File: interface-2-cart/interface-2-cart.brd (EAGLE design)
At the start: 49.5 x 47.9 mm, 37 parts, among them U1 RP2040, U2 SN74LVC245ADBR, U3 W25Q128JVSIQ, U4 SN74LVC245ADBR, U5 SN74LVC245ADBR, X1 TSX-32250

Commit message: New images
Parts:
- added PROG: (no value), adafruit:1X06
- added Q1, Q2: (no value), semicon-smd-ipc:SOT23
- added R1, R10, R11, R12, R13, R14, R15, R16, R17, R18, R19, R2, R20, R5: 1K, rcl:R0402
- added R4, R6: 10K, rcl:R0402
- added RST_BUT: PTS645SM43SMTR92LFS, PTS645SM43SMTR92LFS:PTS645(SMT)
- added S_LED1, S_LED10, S_LED2, S_LED3, S_LED362, S_LED4, S_LED5, S_LED6, S_LED7, S_LED8, S_LED9: 20mA, led-0402:LED_VLMW15_VIS
- moved C2 11.8 mm to (13.5, 15.5)
- moved C3 11.8 mm to (13.6, 27.3)
- moved 3V3_REG2 11.8 mm to (33.8, 29.1)
- moved C11 11.8 mm to (33.8, 26.2)
- moved C8 11.8 mm to (33.8, 32.0)
- moved R9 4.59 mm to (36.3, 34.8), turned to 90 degrees
- moved C18 3.42 mm to (1.52, 29.0), turned to 90 degrees
- moved R8 2.97 mm to (36.2, 43.2), turned to 90 degrees
- moved RUN_BUT 1.91 mm to (41.8, 34.5)
- moved C5 0.64 mm to (24.4, 36.4)
- moved X1 0.64 mm to (23.7, 32.5)
- moved C1 0.63 mm to (26.9, 32.9)
- moved C9 0.63 mm to (22.1, 36.2)
- moved BOOT_BUT 0.51 mm to (41.7, 43.2)
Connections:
- removed net BUT: U1.34
- removed net RESET_5V: U5.2
- removed net ROMCS: U1.39, U2.1
- new net /CARTCS: R1.1, R6.2, S_LED8.C, U1.39
- new net /RESET: PROG.4, Q2.3, R4.2, RST_BUT.3
- new net CARTCS: Q1.3, R5.2, U$1./ROMCS, U2.1
- new net L0: R10.1, S_LED7.A
- new net L1: R11.1, S_LED6.A
- new net L2: R12.1, S_LED5.A
- new net L3: R13.1, S_LED4.A
- new net L4: R14.1, S_LED3.A
- new net L5: R15.1, S_LED2.A
- new net L6: R16.1, S_LED1.A
- new net L7: R17.1, S_LED362.A
- new net N$1: Q1.1, R1.2
- new net N$2: Q2.1, R2.2
- new net N$4: R18.1, S_LED8.A
- new net N$5: R19.1, S_LED9.A
- new net N$6: R20.1, S_LED10.A
- new net SWCLK: PROG.2, U1.24
- new net SWD: PROG.3, U1.25
- new net USER_LED: R20.2, U1.34
- net 3V3: now also PROG.1, R6.1; no longer C2.2, U2.20
- net D0: now also R10.2
- net D1: now also R11.2
- net D2: now also R12.2
- net D3: now also R13.2
- net D4: now also R14.2
- net D5: now also R15.2
- net D6: now also R16.2
- net D7: now also R17.2
- net GND: now also PROG.6, Q1.2, Q2.2, RST_BUT.1, S_LED1.C, S_LED10.C, S_LED2.C, S_LED3.C, S_LED362.C, S_LED4.C, S_LED5.C, S_LED6.C, S_LED7.C, U5.18
- net RESET: now also R2.1; no longer U5.18
- net ROMRQ_5V: now also S_LED9.C
- net VCC: now also C2.2, PROG.5, R18.2, R19.2, R4.1, R5.1, U2.20; no longer U$1./ROMCS
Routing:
- net CARTCS: track 0.00 -> 65.1 mm, vias 0 -> 2
- net USER_LED: track 0.00 -> 61.4 mm, vias 0 -> 4
- net /CARTCS: track 0.00 -> 51.3 mm, vias 0 -> 2
- net VCC: track 102.4 -> 61.6 mm, vias 4 -> 8
- net RESET: track 44.4 -> 12.7 mm
- net /RESET: track 0.00 -> 27.0 mm
- net ROMRQ_5V: track 7.15 -> 27.2 mm, vias 0 -> 2
- net GND: track 66.2 -> 86.2 mm, vias 36 -> 40
- net ROMCS: track 18.4 -> 0.00 mm, vias 2 -> 0
- net SWD: track 0.00 -> 13.4 mm
- net D7: track 22.8 -> 36.1 mm
- net L4: track 0.00 -> 12.9 mm, vias 0 -> 2
- net SWCLK: track 0.00 -> 12.6 mm
- net D6: track 24.2 -> 35.7 mm
- net L5: track 0.00 -> 11.5 mm, vias 0 -> 2
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- added copper zone on layer 15, net VCC
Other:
- outline, holes or cut-outs redrawn
- board text added: "/ROMCS"
- board text added: "/ROMRQ"
- board text added: "3V3"
- board text added: "5V"
- board text added: "CLK"
- board text added: "DATA"
- board text added: "GND"
- board text added: "RP BOOT"
- board text added: "RP RUN"
- board text added: "SWD"
- board text added: "USER"
- board text added: "ZX RST"
- board text added: "ZXR"

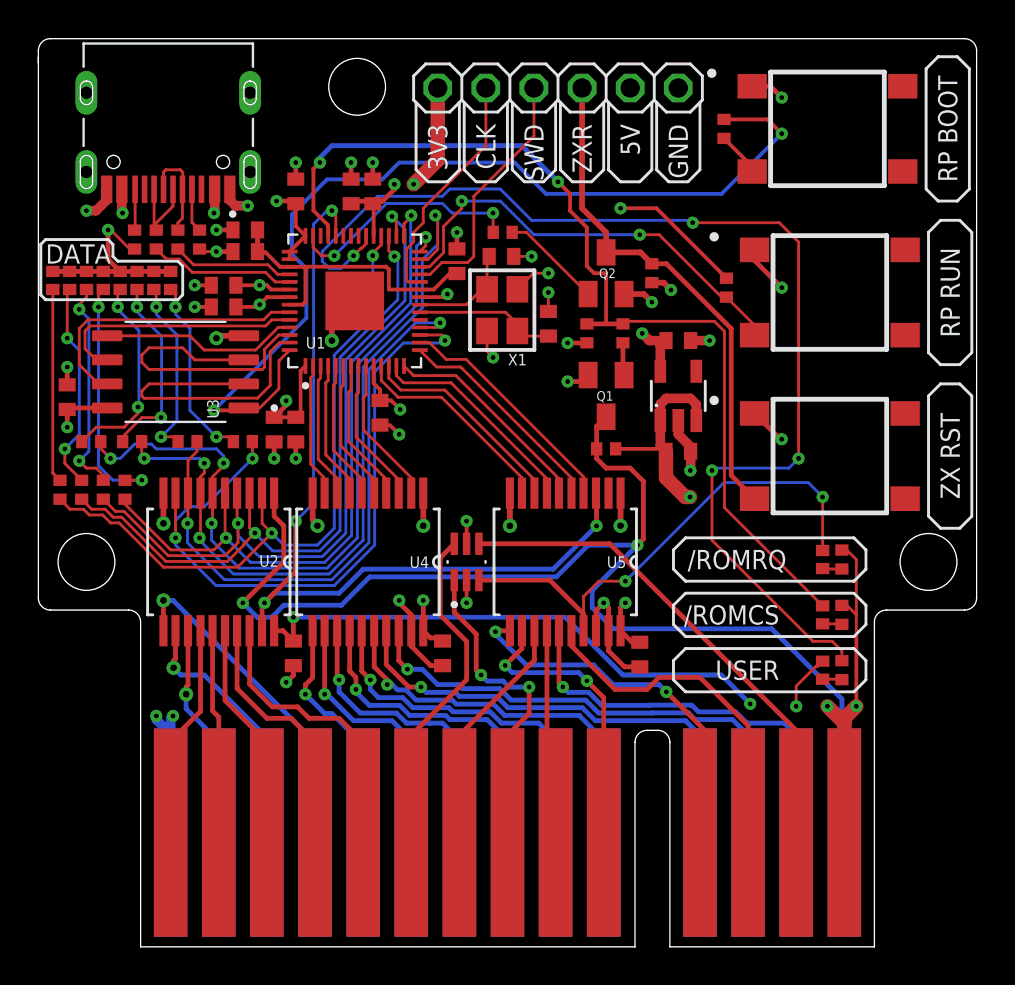
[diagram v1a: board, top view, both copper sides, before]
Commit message: Created initial BOM and mount files, although need to replace one of the octal buffers with a level shifter
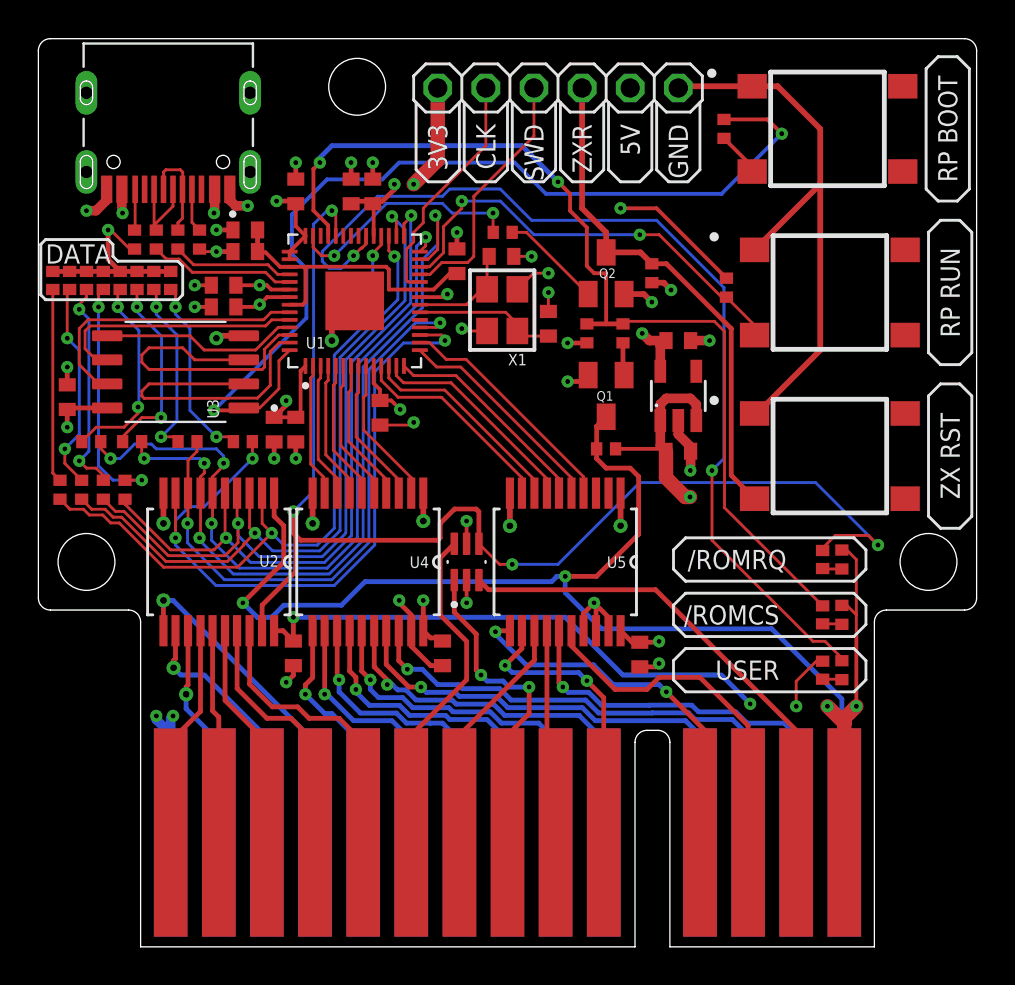
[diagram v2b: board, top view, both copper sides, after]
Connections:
- removed net ROMRQ_5V: S_LED9.C, U$2.3, U5.17
- net A15_5V: now also U$2.3; no longer U$2.4
- net GND: now also U5.17
- net ROMRQ: now also S_LED9.C, U$2.4; no longer U5.3
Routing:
- net ROMRQ_5V: track 27.2 -> 0.00 mm, vias 2 -> 0
- net GND: track 86.2 -> 109.6 mm, vias 40 -> 38
- net ROMRQ: track 46.2 -> 66.2 mm
- net USER_LED: track 61.4 -> 51.8 mm, vias 4 -> 2
- net CARTCS: track 65.1 -> 62.9 mm
- net A15_5V: track 26.2 -> 25.4 mm
- net 3V3: track 52.1 -> 51.6 mm
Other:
- outline, holes or cut-outs redrawn
- board text added: "ZXelerator 2025 Smashcat"

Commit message: Fixed hardware issue! Fixed firmware issue with volatiles not updating - core1 was not starting up!
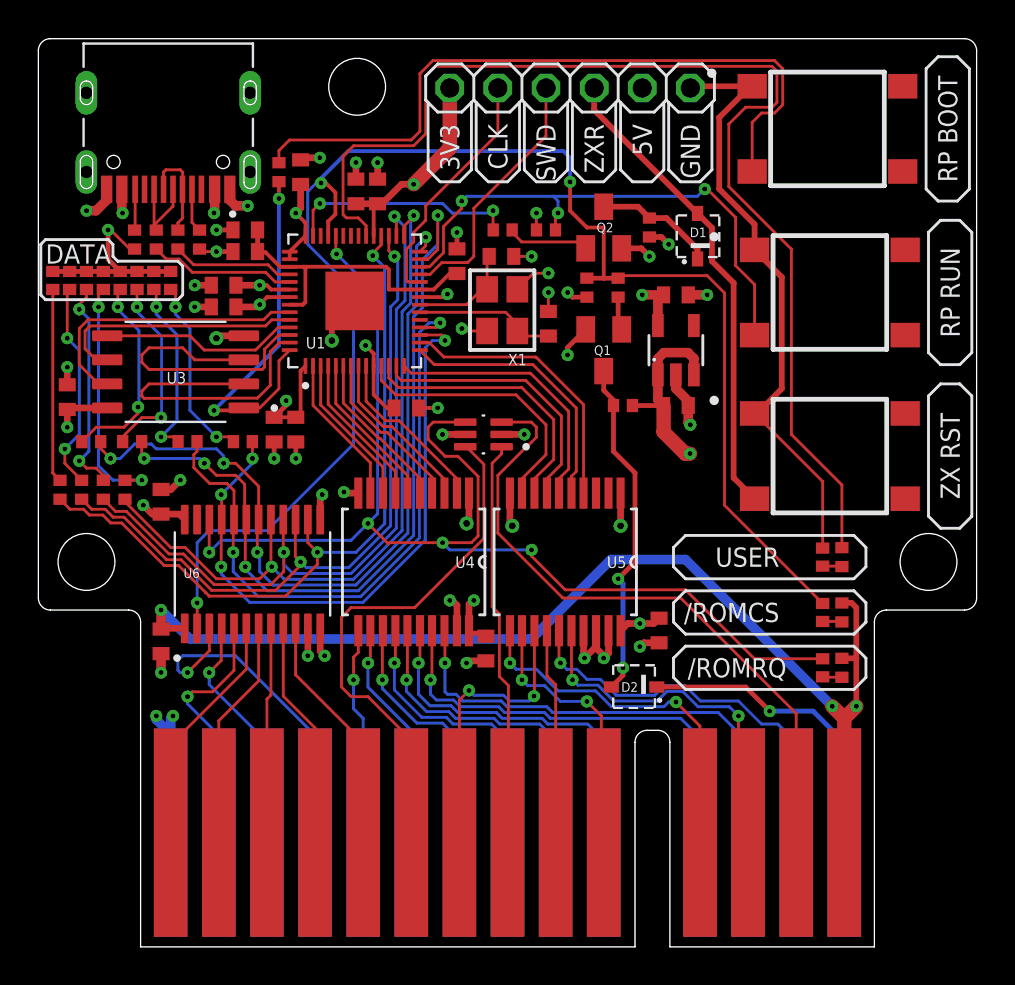
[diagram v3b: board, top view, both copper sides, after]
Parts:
- removed U2: SN74LVC245ADBR, SN74LVC245ADBR:SOP65P780X200-20N
- added C12: 1uF, rcl:C0402
- added D1, D2: BZX384C5V6-E3-08, BZX384C5V6-E3-08:SOD-323
- added U6: SN74LVCC4245APWR, SN74LVCC4245APWR:SOP65P640X120-24N
- R5: value 1K -> 470R
- moved R8 23.6 mm to (12.7, 40.9), turned to 270 degrees
- moved R9 10.0 mm to (26.8, 37.8), turned to 180 degrees
- moved C2 7.01 mm to (6.48, 16.1)
- moved U$2 6.79 mm to (23.5, 27.1), turned to 180 degrees
- moved R20 5.97 mm to (42.4, 20.6)
- moved S_LED10 5.97 mm to (41.4, 20.6)
- moved R19 5.71 mm to (42.4, 14.7)
- moved S_LED9 5.71 mm to (41.4, 14.7)
- moved R5 2.45 mm to (30.9, 28.6)
- moved R1 2.43 mm to (30.6, 34.8)
- moved C8 2.42 mm to (33.7, 34.4)
- moved Q1 2.42 mm to (29.8, 31.5)
- moved 3V3_REG2 2.42 mm to (33.7, 31.5)
- moved C11 2.42 mm to (33.7, 28.6)
- moved Q2 2.42 mm to (29.8, 38.0)
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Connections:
- new net /RESET_PROTECTED: D1.C, Q2.3, R4.2
- new net N$7: D2.C, U$1./ROMCS
- net /CARTCS: now also U6.2
- net /RESET: now also D1.A; no longer Q2.3, R4.2
- net 3V3: now also C12.2, U6.24
- net CARTCS: now also D2.A; no longer U$1./ROMCS, U2.1
- net D0: now also U6.21; no longer U2.9
- net D0_5V: now also U6.3; no longer U2.11
- net D1: now also U6.20; no longer U2.8
- net D1_5V: now also U6.4; no longer U2.12
- net D2: now also U6.19; no longer U2.7
- net D2_5V: now also U6.5; no longer U2.13
- net D3: now also U6.18; no longer U2.6
- net D3_5V: now also U6.6; no longer U2.14
- net D4: now also U6.17; no longer U2.5
- net D4_5V: now also U6.7; no longer U2.15
- net D5: now also U6.16; no longer U2.4
- net D5_5V: now also U6.8; no longer U2.16
- net D6: now also U6.15; no longer U2.3
- net D6_5V: now also U6.9; no longer U2.17
- net D7: now also U6.14; no longer U2.2
- net D7_5V: now also U6.10; no longer U2.18
- net GND: now also C12.1, U6.11, U6.12, U6.13; no longer U2.10
- net ROMRQ: now also U6.22; no longer U2.19
- net VCC: now also U6.1; no longer U2.20
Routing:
- net CARTCS: track 62.9 -> 18.1 mm
- net N$9: track 2.37 -> 37.7 mm
- net QSPI_SS: track 51.2 -> 19.7 mm
- net /CARTCS: track 51.3 -> 81.6 mm, vias 2 -> 3
- net N$7: track 0.00 -> 15.9 mm, vias 0 -> 1
- net VCC: track 61.6 -> 72.2 mm, vias 8 -> 7
- net A14_5V: track 17.3 -> 27.9 mm
- net USER_LED: track 51.8 -> 61.3 mm, vias 2 -> 0
- net A15_5V: track 25.4 -> 34.4 mm
- net /RESET_PROTECTED: track 0.00 -> 6.40 mm
- net RUN: track 23.4 -> 28.6 mm, vias 2 -> 3
- net /MREQ: track 16.6 -> 21.0 mm, vias 2 -> 0
- net D0: track 37.3 -> 33.3 mm, vias 3 -> 4
- net A8: track 11.1 -> 14.6 mm
- net A9: track 11.3 -> 14.6 mm
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
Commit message: New cartridge PCB design, smaller, using RP2350 now. Need to modify more to reduce wings on side, so it's square I think - will give more space in casing
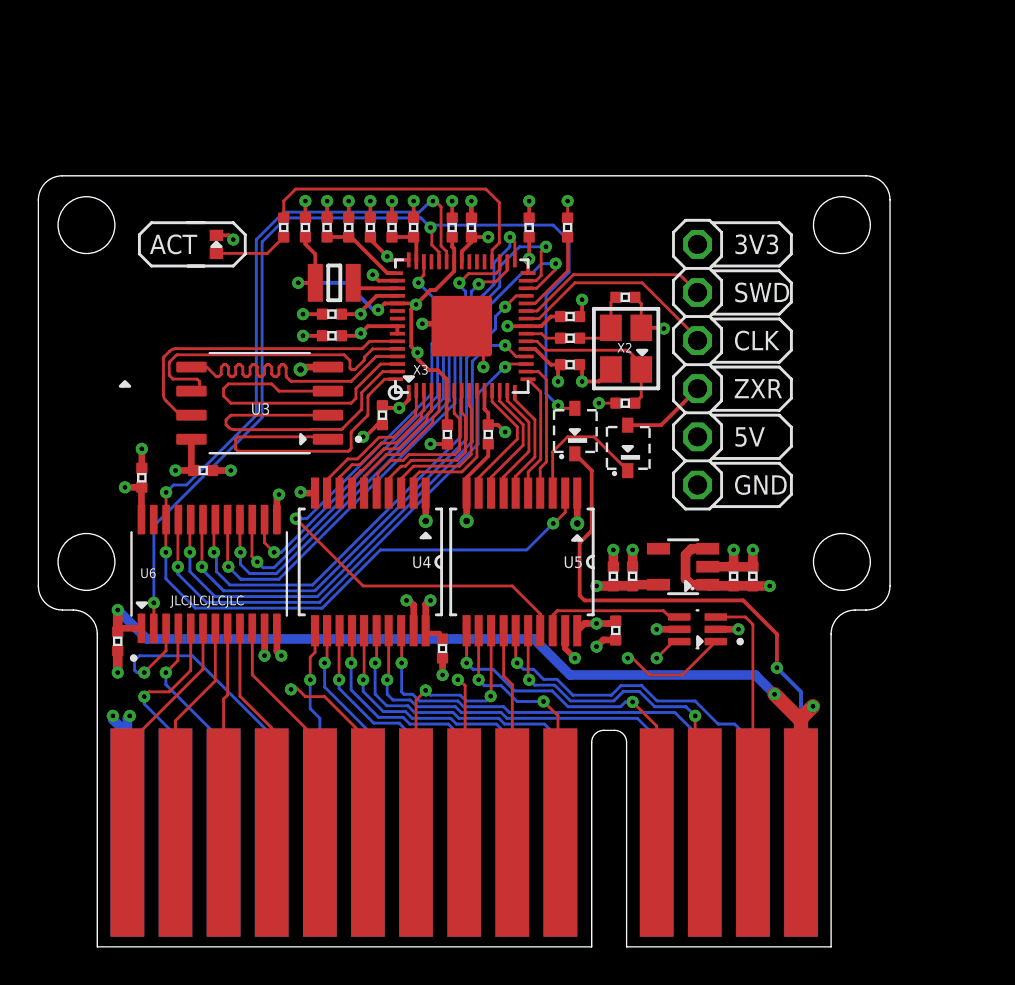
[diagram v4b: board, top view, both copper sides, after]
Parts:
- removed BOOT_BUT, RST_BUT, RUN_BUT: PTS645SM43SMTR92LFS, PTS645SM43SMTR92LFS:PTS645(SMT)
- removed C6, C7: 100nF, rcl:C0402
- removed C9: 1uF, rcl:C0402
- removed D1: BZX384C5V6-E3-08, BZX384C5V6-E3-08:SOD-323
- removed Q1, Q2: (no value), semicon-smd-ipc:SOT23
- removed R1, R10, R11, R12, R13, R14, R15, R16, R17, R18, R19, R2, R8: 1K, rcl:R0402
- removed R21, R22: 5K1, rcl:R0402
- removed R3, R7: 20R, rcl:R0402
- removed R4, R6: 10K, rcl:R0402
- removed R5: 470R, rcl:R0402
- removed S_LED1, S_LED2, S_LED3, S_LED362, S_LED4, S_LED5, S_LED6, S_LED7, S_LED8, S_LED9: 20mA, led-0402:LED_VLMW15_VIS
- removed U1: RP2040, RP2040:QFN40P700X700X90-57N
- removed UPSTREAM_PORT: TYPE-C-31-M-12, TYPE-C-31-M-12:HRO_TYPE-C-31-M-12
- removed X1: TSX-32250, TSX-3225:TSX-3225
- added C13, C14: 15pF, res-small-footprint:C0402
- added C23, C24: 2u2, res-small-footprint:C0402
- added C25, C26, C28: 10uF, res-small-footprint:C0402
- added C27: 100nF, res-small-footprint:C0402
- added D3: BZX384C5V6-E3-08, BZX384C5V6-E3-08:SOD-323
- added L1: DFE252012F-3R3M=P2, microbuilder:INDUCTOR_1007
- added R23: 1K, res-small-footprint:0402
- added R24: 10K, res-small-footprint:0402
- added R25: 10R, res-small-footprint:0402
- added X2: TSX-32250, TSX-3225:TSX-3225
- added X3: DNP, adafruit_micro:QFN60_7MM_REDUCEDEPAD
- C1, C5: value 15pF -> 100nF; device rcl:C0402 -> res-small-footprint:C0402
- C10, C11, C12, C15, C16, C17, C18, C19, C2, C20, C21, C22, C3, C4, C8: device rcl:C0402 -> res-small-footprint:C0402
- R20: device rcl:R0402 -> res-small-footprint:0402
- R9: value 10K -> 10R; device rcl:R0402 -> res-small-footprint:0402
- moved S_LED10 36.0 mm to (9.40, 37.1)
- moved R20 34.2 mm to (13.0, 38.0)
- moved C15 18.5 mm to (28.1, 30.7), turned to 0 degrees
- moved PROG 16.1 mm to (34.8, 30.7), turned to 270 degrees
- moved C16 16.0 mm to (23.7, 27.1), turned to 270 degrees
- moved U$2 15.3 mm to (34.8, 16.8)
- moved C8 15.0 mm to (31.4, 19.6), turned to 90 degrees
- moved C3 14.1 mm to (22.9, 38.0), turned to 270 degrees
- moved D2 13.8 mm to (28.3, 27.2), turned to 90 degrees
- moved C19 11.9 mm to (18.2, 28.1), turned to 270 degrees
- moved R9 11.6 mm to (15.2, 38.0), turned to 90 degrees
- moved C22 11.5 mm to (25.9, 38.0), turned to 90 degrees
- moved 3V3_REG2 11.4 mm to (34.0, 20.1), turned to 90 degrees
- moved C11 9.52 mm to (36.7, 19.6), turned to 90 degrees
- moved C21 8.79 mm to (15.5, 32.3), turned to 180 degrees
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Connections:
- net N$7 renamed /ROMCS
- removed net /CARTCS: R1.1, R6.2, S_LED8.C, U1.39, U6.2
- removed net /RESET_PROTECTED: D1.C, Q2.3, R4.2
- removed net CARTCS: D2.A, Q1.3, R5.2
- removed net L0: R10.1, S_LED7.A
- removed net L1: R11.1, S_LED6.A
- removed net L2: R12.1, S_LED5.A
- removed net L3: R13.1, S_LED4.A
- removed net L4: R14.1, S_LED3.A
- removed net L5: R15.1, S_LED2.A
- removed net L6: R16.1, S_LED1.A
- removed net L7: R17.1, S_LED362.A
- removed net N$1: Q1.1, R1.2
- removed net N$18: R21.2, UPSTREAM_PORT.A5
- removed net N$19: R22.2, UPSTREAM_PORT.B5
- removed net N$2: Q2.1, R2.2
- removed net N$3: R3.1, U1.46
- removed net N$4: R18.1, S_LED8.A
- removed net N$5: R19.1, S_LED9.A
- removed net N$8: R7.1, U1.47
- removed net RESET: R2.1, U1.41
- removed net USB_DM: R3.2, UPSTREAM_PORT.A7, UPSTREAM_PORT.B7
- removed net USB_DP: R7.2, UPSTREAM_PORT.A6, UPSTREAM_PORT.B6
- removed net VREG_OUT_1V1: C6.1, C7.1, C9.1, U1.23, U1.45, U1.50
- new net /RESET_3V3: U5.17, X3.43
- new net /ROMCS_3V3: D2.A, U6.2, X3.41
- new net 1V2: C1.P$1, C27.P$1, C28.P$1, C5.P$1, L1.P$1, X3.23, X3.39, X3.50, X3.6
- new net N$10: R23.P$2, X3.22
- new net N$11: L1.P$2, X3.48
- new net N$12: C23.P$1, R9.P$1, X3.46
- new net N$13: C24.P$1, R25.P$1, X3.44
- new net ROMRQ_3V3: U5.2, U6.22, X3.40
- net /RESET: now also D3.A; no longer D1.A, RST_BUT.3
- net 3V3: now also C10.P$1, C12.P$2, C15.P$1, C16.P$1, C17.P$1, C18.P$1, C19.P$1, C20.P$1, C21.P$1, C22.P$1, C26.P$1, C3.P$2, C4.P$2, C8.P$1, R24.P$2, R25.P$2, R9.P$2, X3.1, X3.11, X3.20, X3.30, X3.38, X3.45, X3.49, X3.53, X3.54; no longer C10.1, C12.2, C15.1, C16.1, C17.1, C18.1, C19.1, C20.1, C21.1, C22.1, C3.2, C4.2, C8.1, R6.1, R9.2, U1.1, U1.10, U1.22, U1.33, U1.42, U1.43, U1.44, U1.48, U1.49
- net A0: now also X3.2; no longer U1.2
- net A1: now also X3.3; no longer U1.3
- net A10: now also X3.14; no longer U1.13
- net A11: now also X3.15; no longer U1.14
- net A12: now also X3.16; no longer U1.15
- net A13: now also X3.17; no longer U1.16
- net A2: now also X3.4; no longer U1.4
- net A3: now also X3.5; no longer U1.5
- net A4: now also X3.7; no longer U1.6
- net A5: now also X3.8; no longer U1.7
- net A6: now also X3.9; no longer U1.8
- net A7: now also X3.10; no longer U1.9
- net A8: now also X3.12; no longer U1.11
- net A9: now also X3.13; no longer U1.12
- net D0: now also X3.18; no longer R10.2, U1.17
- net D1: now also X3.19; no longer R11.2, U1.18
- net D2: now also X3.27; no longer R12.2, U1.27
- net D3: now also X3.28; no longer R13.2, U1.28
- net D4: now also X3.29; no longer R14.2, U1.29
- net D5: now also X3.31; no longer R15.2, U1.30
- net D6: now also X3.32; no longer R16.2, U1.31
- net D7: now also X3.33; no longer R17.2, U1.32
- net GND: now also C1.P$2, C10.P$2, C11.P$2, C12.P$1, C13.P$2, C14.P$2, C15.P$2, C16.P$2, C17.P$2, C18.P$2, C19.P$2, C2.P$1, C20.P$2, C21.P$2, C22.P$2, C23.P$2, C24.P$2, C25.P$2, C26.P$2, C27.P$2, C28.P$2, C3.P$1, C4.P$1, C5.P$2, C8.P$2, X2.2, X2.4, X3.47, X3.P$1; no longer BOOT_BUT.1, C1.2, C10.2, C11.2, C12.1, C15.2, C16.2, C17.2, C18.2, C19.2, C2.1, C20.2, C21.2, C22.2, C3.1, C4.1, C5.2, C6.2, C7.2, C8.2, C9.2, Q1.2, Q2.2, R21.1, R22.1, RST_BUT.1, RUN_BUT.1, S_LED1.C, S_LED2.C, S_LED3.C, S_LED362.C, S_LED4.C, S_LED5.C, S_LED6.C, S_LED7.C, U1.57, U5.17, U5.18, UPSTREAM_PORT.A1B12, UPSTREAM_PORT.B1A12, X1.2, X1.4
- net N$6: now also R20.P$1; no longer R20.1
- net N$9: now also D3.C, U5.3; no longer BOOT_BUT.3, R8.1
- net QSPI_SCLK: now also X3.56; no longer U1.52
- net QSPI_SD0: now also X3.57; no longer U1.53
- net QSPI_SD1: now also X3.59; no longer U1.55
- net QSPI_SD2: now also X3.58; no longer U1.54
- net QSPI_SD3: now also X3.55; no longer U1.51
- net QSPI_SS: now also X3.60; no longer R8.2, U1.56
- net ROMRQ: now also U5.18; no longer S_LED9.C, U1.38, U6.22
- net RUN: now also R24.P$1, X3.26; no longer R9.1, RUN_BUT.3, U1.26
- net SWCLK: now also PROG.3, X3.24; no longer PROG.2, U1.24
- net SWD: now also PROG.2, X3.25; no longer PROG.3, U1.25
- net USER_LED: now also R20.P$2, X3.34; no longer R20.2, U1.34
- net VCC: now also C11.P$1, C2.P$2, C25.P$1; no longer C11.1, C2.2, R18.2, R19.2, R4.1, R5.1, UPSTREAM_PORT.A4B9, UPSTREAM_PORT.B4A9
- net XIN: now also C13.P$1, X2.1, X3.21; no longer C1.1, U1.20, X1.1
- net XOUT: now also C14.P$1, R23.P$1, X2.3; no longer C5.1, U1.21, X1.3
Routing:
- net /CARTCS: track 81.6 -> 0.00 mm, vias 3 -> 0
- net ROMRQ_3V3: track 0.00 -> 58.9 mm, vias 0 -> 4
- net ROMRQ: track 65.6 -> 7.73 mm, vias 5 -> 0
- net /ROMCS_3V3: track 0.00 -> 52.5 mm, vias 0 -> 3
- net USER_LED: track 61.3 -> 16.1 mm
- net GND: track 111.2 -> 68.1 mm, vias 42 -> 41
- net /RESET_3V3: track 0.00 -> 33.4 mm, vias 0 -> 2
- net 1V2: track 0.00 -> 31.0 mm, vias 0 -> 5
- net N$9: track 37.7 -> 7.21 mm
- net RUN: track 28.6 -> 4.69 mm, vias 3 -> 0
- net A15_5V: track 34.4 -> 13.1 mm
- net /RESET: track 25.2 -> 4.48 mm
- net CARTCS: track 18.1 -> 0.00 mm, vias 2 -> 0
- net VCC: track 72.2 -> 55.2 mm, vias 7 -> 4
- net VREG_OUT_1V1: track 16.3 -> 0.00 mm
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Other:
- board size 49.5 x 47.9 mm -> 45 x 40.7 mm
- board text added: "ACT"
- board text added: "JLCJLCJLCJLC"
- board text removed: "/ROMCS"
- board text removed: "/ROMRQ"
- board text removed: "DATA"
- board text removed: "RP BOOT"
- board text removed: "RP RUN"
- board text removed: "USER"
- board text removed: "ZX RST"

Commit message: PCB design completed and submitted for production
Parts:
- removed PROG: (no value), adafruit:1X06
- added JP2: (no value), pinhead:1X05
- moved S_LED10 3.27 mm to (6.29, 38.1)
- moved C26 3.24 mm to (27.1, 19.6)
- moved 3V3_REG2 3.11 mm to (30.9, 20.1)
- moved D2 3.11 mm to (25.2, 27.2)
- moved R24 3.11 mm to (24.8, 38.0)
- moved U$2 3.11 mm to (31.7, 16.8)
- moved C19 3.11 mm to (15.0, 28.1)
- moved C24 3.11 mm to (15.6, 38.0)
- moved L1 3.11 mm to (12.5, 35.1)
- moved R20 3.11 mm to (9.84, 38.0)
- moved C12 3.11 mm to (2.35, 24.8)
- moved C18 3.11 mm to (5.59, 25.1)
- moved C2 3.11 mm to (1.08, 16.1)
- moved C1 3.11 mm to (25.0, 33.3)
- moved C10 3.11 mm to (12.4, 33.4)
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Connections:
- net /RESET: now also JP2.4; no longer PROG.4
- net 3V3: now also JP2.1; no longer PROG.1
- net GND: now also JP2.5; no longer PROG.6
- net SWCLK: now also JP2.3; no longer PROG.3
- net SWD: now also JP2.2; no longer PROG.2
- net VCC: no longer PROG.5
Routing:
- net ROMRQ_3V3: track 58.9 -> 57.4 mm
- net /ROMCS_3V3: track 52.5 -> 51.8 mm
- net SWCLK: track 11.2 -> 10.6 mm
- net USER_LED: track 16.1 -> 16.7 mm, vias 0 -> 2
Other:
- board size 45 x 40.7 mm -> 38.7 x 40.1 mm
- board text added: "ZXelerator V1.0 2025 Smashcat"
- board text removed: "5V"
- board text removed: "ZXelerator 2025 Smashcat"
